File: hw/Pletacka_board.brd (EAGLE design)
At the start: 75 x 55 mm, 45 parts, among them U1 LM75BDP, U2 EL357N(A)(TA)-G, U3 EL357N(A)(TA)-G, U4 EL357N(A)(TA)-G, U5 EL357N(A)(TA)-G, U6 TPS54231D

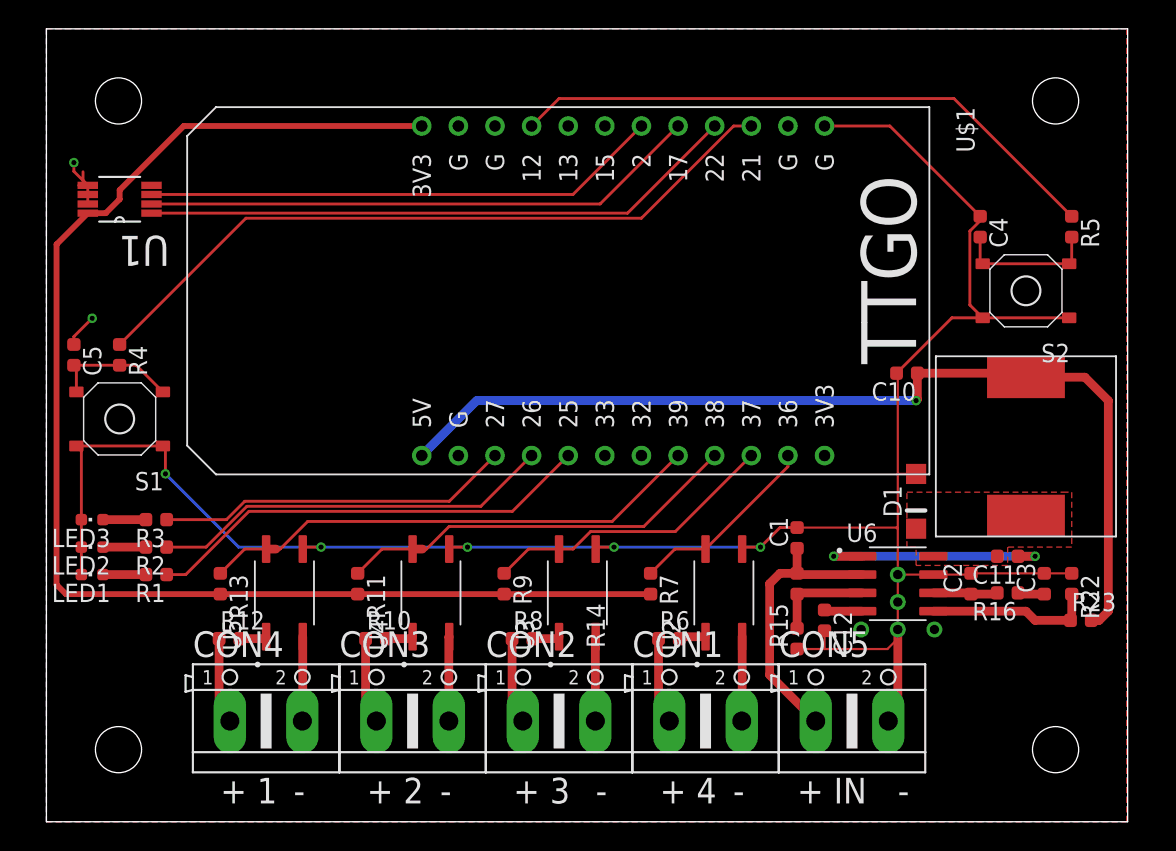
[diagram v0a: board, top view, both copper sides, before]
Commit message: Add 2 pinheads
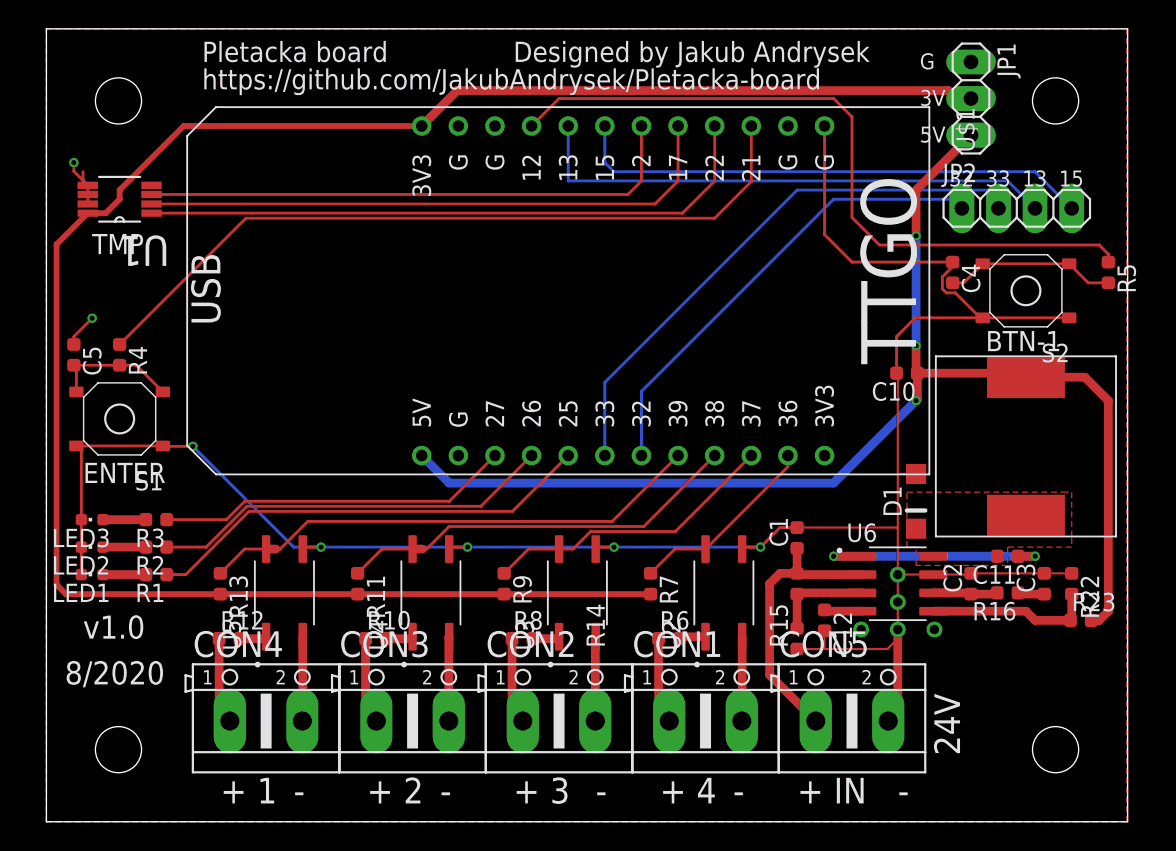
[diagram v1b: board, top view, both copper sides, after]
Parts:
- added JP1: (no value), pinhead:1X03
- added JP2: (no value), pinhead:1X04
- moved R5 4.07 mm to (73.7, 38.1)
- moved C4 3.70 mm to (62.9, 38.1)
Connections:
- removed net N$26: U$1.15
- removed net N$27: U$1.13
- removed net N$3: U$1.32
- removed net N$4: U$1.33
- new net GPIO13: JP2.3, U$1.13
- new net GPIO15: JP2.4, U$1.15
- new net GPIO32: JP2.1, U$1.32
- new net GPIO33: JP2.2, U$1.33
- net +3V3: now also JP1.2
- net +5V: now also JP1.3
- net GND: now also JP1.1
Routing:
- net +3V3: track 94.2 -> 133.5 mm
- net GPIO33: track 0.00 -> 38.8 mm
- net GPIO13: track 0.00 -> 37.0 mm
- net GPIO15: track 0.00 -> 36.2 mm
- net GPIO32: track 0.00 -> 32.5 mm
- net +5V: track 68.5 -> 88.2 mm, vias 1 -> 3
- net BUTTON2: track 41.6 -> 49.9 mm
- net BUTTON1: track 50.1 -> 52.4 mm
- net TMP_OS: track 36.0 -> 38.2 mm
- net TMP_SDA: track 41.6 -> 43.8 mm
- net TMP_SCL: track 38.8 -> 41.0 mm
- net GND: track 164.9 -> 167.1 mm
- net N$10: track 9.84 -> 11.9 mm
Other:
- board text added: "13"
- board text added: "15"
- board text added: "24V"
- board text added: "32"
- board text added: "33"
- board text added: "3V"
- board text added: "5V"
- board text added: "8/2020"
- board text added: "BTN-1"
- board text added: "Designed by Jakub Andrysek"
- board text added: "ENTER"
- board text added: "G"
- board text added: "Pletacka board"
- board text added: "TMP"
- board text added: "USB"
- board text added: "https://github.com/JakubAndrysek/Pletacka-board"
- board text added: "v1.0"

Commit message: Fix Cednik's issues
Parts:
- added D2, D4, D6: B5819W, B5819W:SOD-123
- added D3: SS34, diode:SMA
- added JP3: (no value), pinhead:1X04
- C1: value 10u -> 10u/50V; device rcl_upravena:C0603 -> rcl_upravena:C1206
- C4, C5: value 1u -> 100n
- R10, R12, R6, R8: value 1k -> 2k/0.25W; device rcl_upravena:R0603 -> rcl_upravena:R1206
- U1: value LM75BDP -> LM75BDP-NEW; device LM75BDP:SOP65P490X110-8N -> LM75BDP:SOT505-1
- moved D1 25.5 mm to (36.8, 12.3), turned to 0 degrees
- moved R13 2.69 mm to (14.0, 18.4)
- moved C1 2.07 mm to (53.6, 21.1), turned to 0 degrees
- moved R8 2.01 mm to (32.4, 14.6)
- moved U3 2.01 mm to (37.5, 17.8)
- moved R12 2.01 mm to (12.1, 14.6)
- moved R10 2.01 mm to (22.2, 14.6)
- moved R6 2.01 mm to (42.5, 14.6)
- moved U2 2.01 mm to (47.6, 17.8)
- moved U4 2.01 mm to (27.3, 17.8)
- moved U5 2.01 mm to (17.1, 17.8)
- moved R7 2.01 mm to (42.5, 18.4)
- moved R11 2.01 mm to (22.2, 18.4)
- moved R9 2.01 mm to (32.4, 18.4)
- moved R5 1.27 mm to (73.7, 36.8)
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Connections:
- net +3V3: now also U$1.3V3-2
- net GND: now also D3.A, JP3.1, JP3.2, JP3.3, JP3.4, U$1.G-2, U$1.G-3, U$1.G-4, U$1.G-5; no longer D1.A
- net N$14: now also D1.A
- net N$15: now also D1.C
- net N$17: now also D2.A
- net N$18: now also D2.C
- net N$20: now also D4.A
- net N$21: now also D4.C
- net N$7: now also D6.A
- net N$9: now also D6.C
- net PH: now also D3.C; no longer D1.C
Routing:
- net GND: track 167.1 -> 96.5 mm, vias 10 -> 12
- net +3V3: track 133.5 -> 108.0 mm
- net N$15: track 1.88 -> 5.14 mm
- net N$9: track 1.88 -> 5.14 mm
- net N$18: track 1.88 -> 5.04 mm
- net N$21: track 1.88 -> 5.04 mm
- net OPTO4: track 35.8 -> 33.3 mm
- net N$10: track 11.9 -> 14.4 mm
- net GPIO13: track 37.0 -> 34.5 mm
- net N$19: track 6.02 -> 8.50 mm
- net N$16: track 6.02 -> 8.50 mm
- net N$6: track 6.02 -> 8.50 mm
- net N$13: track 6.02 -> 8.50 mm
- net N$17: track 5.86 -> 8.22 mm
- net N$7: track 5.86 -> 8.03 mm
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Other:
- outline, holes or cut-outs redrawn
- board text added: "Designed by kubaandrysek.cz"
- board text added: "PWR"
- board text added: "SEND"
- board text added: "WIFI"
- board text removed: "BTN-1"
- board text removed: "Designed by Jakub Andrysek"

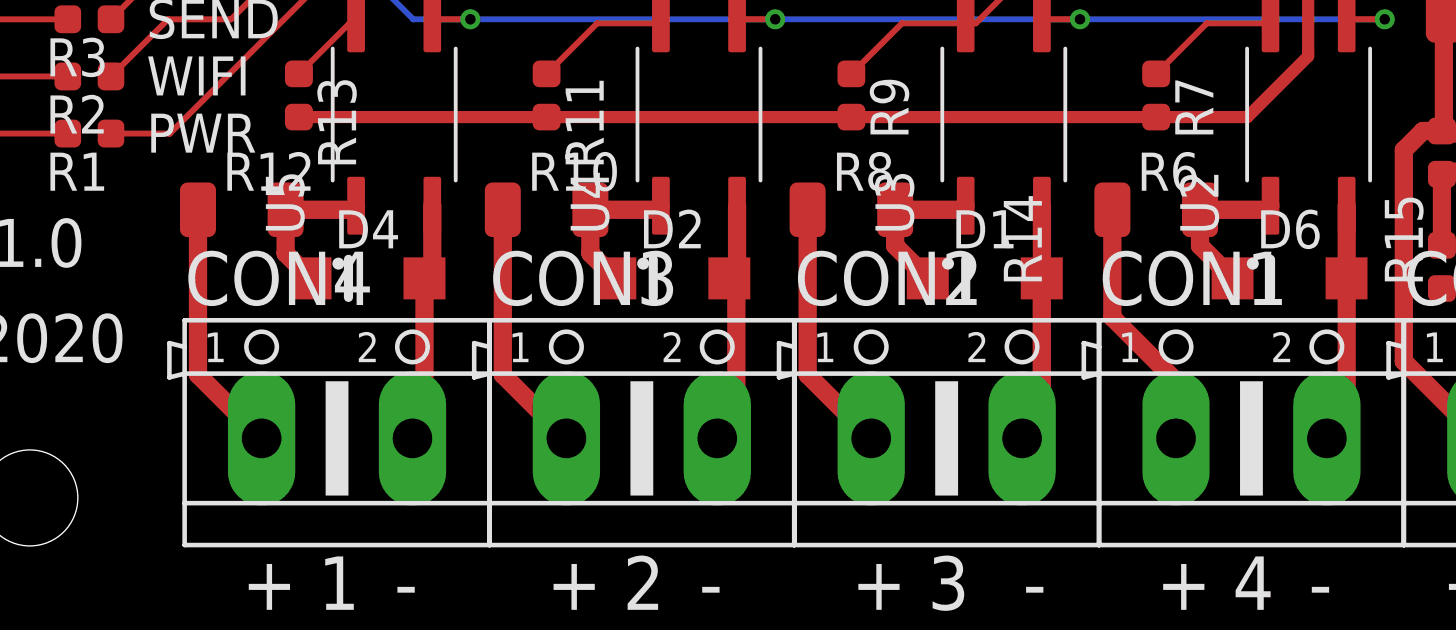
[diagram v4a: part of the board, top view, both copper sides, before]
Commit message: Change octocoupler resistor to 20k (close #2)
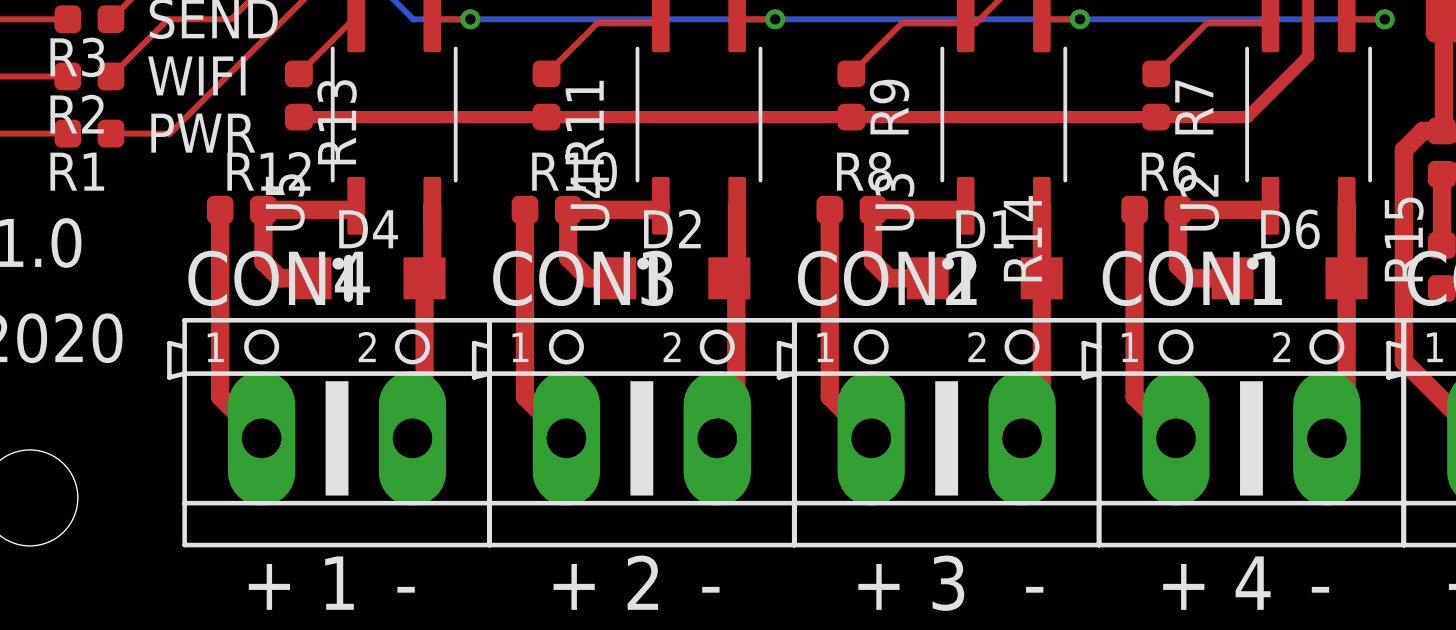
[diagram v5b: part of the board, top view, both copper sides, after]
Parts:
- R10, R12, R6, R8: value 2k/0.25W -> 20k; device rcl_upravena:R1206 -> rcl_upravena:R0603
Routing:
- net N$9: track 5.14 -> 7.01 mm
- net N$15: track 5.14 -> 6.93 mm
- net N$21: track 5.04 -> 6.68 mm
- net N$18: track 5.04 -> 6.61 mm
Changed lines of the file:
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@@
 <attribute name="VALUE" x="40.64" y="1.27" size="1.778" layer="27" ratio="10"/>
 </element>
-<element name="R6" library="rcl_upravena" package="R1206" value="2k/0.25W" x="42.545" y="14.605" smashed="yes">
-<attribute name="LCSC_ID" value="C17944" x="42.545" y="14.605" size="1.778" layer="27" display="off"/>
+<element name="R6" library="rcl_upravena" package="R0603" value="20k" x="42.545" y="14.605" smashed="yes">
+<attribute name="LCSC_ID" value="C4184" x="42.545" y="14.605" size="1.778" layer="27" display="off"/>
 <attribute name="NAME" x="41.91" y="15.24" size="1.27" layer="25"/>
 <attribute name="VALUE" x="41.91" y="12.7" size="1.27" layer="27"/>
@@
 <attribute name="VALUE" x="30.48" y="1.27" size="1.778" layer="27" ratio="10"/>
 </element>
-<element name="R8" library="rcl_upravena" package="R1206" value="2k/0.25W" x="32.385" y="14.605" smashed="yes">
-<attribute name="LCSC_ID" value="C17944" x="32.385" y="14.605" size="1.778" layer="27" display="off"/>
+<element name="R8" library="rcl_upravena" package="R0603" value="20k" x="32.385" y="14.605" smashed="yes">
+<attribute name="LCSC_ID" value="C4184" x="32.385" y="14.605" size="1.778" layer="27" display="off"/>
 <attribute name="NAME" x="31.75" y="15.24" size="1.27" layer="25"/>
 <attribute name="VALUE" x="31.75" y="12.7" size="1.27" layer="27"/>
@@
 <attribute name="VALUE" x="20.32" y="1.27" size="1.778" layer="27" ratio="10"/>
 </element>
-<element name="R10" library="rcl_upravena" package="R1206" value="2k/0.25W" x="22.225" y="14.605" smashed="yes">
-<attribute name="LCSC_ID" value="C17944" x="22.225" y="14.605" size="1.778" layer="27" display="off"/>
+<element name="R10" library="rcl_upravena" package="R0603" value="20k" x="22.225" y="14.605" smashed="yes">
+<attribute name="LCSC_ID" value="C4184" x="22.225" y="14.605" size="1.778" layer="27" display="off"/>
 <attribute name="NAME" x="21.59" y="15.24" size="1.27" layer="25"/>
 <attribute name="VALUE" x="21.59" y="12.7" size="1.27" layer="27"/>
@@
 <attribute name="VALUE" x="10.16" y="1.27" size="1.778" layer="27" ratio="10"/>
 </element>
-<element name="R12" library="rcl_upravena" package="R1206" value="2k/0.25W" x="12.065" y="14.605" smashed="yes">
-<attribute name="LCSC_ID" value="C17944" x="12.065" y="14.605" size="1.778" layer="27" display="off"/>
+<element name="R12" library="rcl_upravena" package="R0603" value="20k" x="12.065" y="14.605" smashed="yes">
+<attribute name="LCSC_ID" value="C4184" x="12.065" y="14.605" size="1.778" layer="27" display="off"/>
 <attribute name="NAME" x="11.43" y="15.24" size="1.27" layer="25"/>
 <attribute name="VALUE" x="11.43" y="12.7" size="1.27" layer="27"/>
@@
 <contactref element="CON1" pad="1"/>
 <contactref element="R6" pad="1"/>
-<wire x1="43.2054" y1="8.893990625" x2="43.2054" y2="6.985" width="0.6096" layer="1"/>
-<wire x1="41.085" y1="14.605" x2="41.085" y2="11.014390625" width="0.6096" layer="1"/>
-<wire x1="41.085" y1="11.014390625" x2="43.2054" y2="8.893990625" width="0.6096" layer="1"/>
+<wire x1="43.2054" y1="6.985" x2="41.825" y2="8.3654" width="0.6096" layer="1"/>
+<wire x1="41.825" y1="8.3654" x2="41.825" y2="14.605" width="0.6096" layer="1"/>
 </signal>
 <signal name="N$7">
@@
 <contactref element="D6" pad="C"/>
 <wire x1="46.355" y1="14.74" x2="46.22" y2="14.605" width="0.6096" layer="1"/>
-<wire x1="46.22" y1="14.605" x2="44.005" y2="14.605" width="0.6096" layer="1"/>
-<wire x1="44.005" y1="14.605" x2="44.005" y2="13.404" width="0.6096" layer="1"/>
-<wire x1="44.005" y1="13.404" x2="45.09" y2="12.319" width="0.6096" layer="1"/>
+<wire x1="46.22" y1="14.605" x2="43.265" y2="14.605" width="0.6096" layer="1"/>
+<wire x1="45.09" y1="12.319" x2="43.688" y2="12.319" width="0.6096" layer="1"/>
+<wire x1="43.265" y1="12.742" x2="43.265" y2="14.605" width="0.6096" layer="1"/>
+<wire x1="43.688" y1="12.319" x2="43.265" y2="12.742" width="0.6096" layer="1"/>
 </signal>
 <signal name="N$13">
 <contactref element="CON2" pad="1"/>
 <contactref element="R8" pad="1"/>
-<wire x1="30.925" y1="14.605" x2="30.925" y2="9.1054" width="0.6096" layer="1"/>
-<wire x1="30.925" y1="9.1054" x2="33.0454" y2="6.985" width="0.6096" layer="1"/>
+<wire x1="33.0454" y1="6.985" x2="31.665" y2="8.3654" width="0.6096" layer="1"/>
+<wire x1="31.665" y1="8.3654" x2="31.665" y2="14.605" width="0.6096" layer="1"/>
 </signal>
 <signal name="N$14">
@@
 <contactref element="U3" pad="1"/>
 <wire x1="36.195" y1="14.74" x2="36.06" y2="14.605" width="0.6096" layer="1"/>
-<wire x1="36.06" y1="14.605" x2="33.845" y2="14.605" width="0.6096" layer="1"/>
+<wire x1="36.06" y1="14.605" x2="33.105" y2="14.605" width="0.6096" layer="1"/>
 <contactref element="D1" pad="C"/>
-<wire x1="33.845" y1="14.605" x2="33.845" y2="13.404" width="0.6096" layer="1"/>
-<wire x1="33.845" y1="13.404" x2="34.93" y2="12.319" width="0.6096" layer="1"/>
+<wire x1="34.93" y1="12.319" x2="33.655" y2="12.319" width="0.6096" layer="1"/>
+<wire x1="33.105" y1="12.869" x2="33.105" y2="14.605" width="0.6096" layer="1"/>
+<wire x1="33.655" y1="12.319" x2="33.105" y2="12.869" width="0.6096" layer="1"/>
 </signal>
 <signal name="N$16">
 <contactref element="CON3" pad="1"/>
 <contactref element="R10" pad="1"/>
-<wire x1="20.765" y1="14.605" x2="20.765" y2="9.1054" width="0.6096" layer="1"/>
-<wire x1="20.765" y1="9.1054" x2="22.8854" y2="6.985" width="0.6096" layer="1"/>
+<wire x1="21.505" y1="14.605" x2="21.505" y2="8.3654" width="0.6096" layer="1"/>
+<wire x1="21.505" y1="8.3654" x2="22.8854" y2="6.985" width="0.6096" layer="1"/>
 </signal>
 <signal name="N$17">
@@
 <contactref element="D2" pad="C"/>
 <wire x1="26.035" y1="14.74" x2="25.9" y2="14.605" width="0.6096" layer="1"/>
-<wire x1="25.9" y1="14.605" x2="23.685" y2="14.605" width="0.6096" layer="1"/>
-<wire x1="23.685" y1="14.605" x2="23.685" y2="13.15" width="0.6096" layer="1"/>
-<wire x1="23.685" y1="13.15" x2="24.516" y2="12.319" width="0.6096" layer="1"/>
+<wire x1="25.9" y1="14.605" x2="22.945" y2="14.605" width="0.6096" layer="1"/>
+<wire x1="24.516" y1="12.319" x2="23.622" y2="12.319" width="0.6096" layer="1"/>
+<wire x1="22.945" y1="12.996" x2="22.945" y2="14.605" width="0.6096" layer="1"/>
+<wire x1="23.622" y1="12.319" x2="22.945" y2="12.996" width="0.6096" layer="1"/>
 </signal>
 <signal name="N$19">
 <contactref element="CON4" pad="1"/>
 <contactref element="R12" pad="1"/>
-<wire x1="10.605" y1="14.605" x2="10.605" y2="9.1054" width="0.6096" layer="1"/>
-<wire x1="10.605" y1="9.1054" x2="12.7254" y2="6.985" width="0.6096" layer="1"/>
+<wire x1="12.7254" y1="6.985" x2="11.345" y2="8.3654" width="0.6096" layer="1"/>
+<wire x1="11.345" y1="8.3654" x2="11.345" y2="14.605" width="0.6096" layer="1"/>
 </signal>
 <signal name="N$20">
@@
 <contactref element="D4" pad="C"/>
 <wire x1="15.875" y1="14.74" x2="15.74" y2="14.605" width="0.6096" layer="1"/>
-<wire x1="15.74" y1="14.605" x2="13.525" y2="14.605" width="0.6096" layer="1"/>
-<wire x1="13.525" y1="14.605" x2="13.525" y2="13.15" width="0.6096" layer="1"/>
-<wire x1="13.525" y1="13.15" x2="14.356" y2="12.319" width="0.6096" layer="1"/>
+<wire x1="15.74" y1="14.605" x2="12.785" y2="14.605" width="0.6096" layer="1"/>
+<wire x1="14.356" y1="12.319" x2="13.335" y2="12.319" width="0.6096" layer="1"/>
+<wire x1="12.785" y1="12.869" x2="12.785" y2="14.605" width="0.6096" layer="1"/>
+<wire x1="13.335" y1="12.319" x2="12.785" y2="12.869" width="0.6096" layer="1"/>
 </signal>
 <signal name="VIN">

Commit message: Change step-down voltage (close #4)
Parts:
- R22: value 1.8k -> 6k8
- R23: value 10k -> 36k
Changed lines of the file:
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@@
 <attribute name="VALUE" x="60.325" y="33.02" size="1.27" layer="27" rot="R180"/>
 </element>
-<element name="R22" library="rcl_upravena" package="R0603" value="1.8k" x="71.12" y="16.51" smashed="yes" rot="R270">
-<attribute name="LCSC_ID" value="C4177" x="71.12" y="16.51" size="1.778" layer="27" rot="R270" display="off"/>
+<element name="R22" library="rcl_upravena" package="R0603" value="6k8" x="71.12" y="16.51" smashed="yes" rot="R270">
+<attribute name="LCSC_ID" value="C23212" x="71.12" y="16.51" size="1.778" layer="27" rot="R270" display="off"/>
 <attribute name="NAME" x="71.755" y="17.145" size="1.27" layer="25" rot="R270"/>
 <attribute name="VALUE" x="69.215" y="17.145" size="1.27" layer="27" rot="R270"/>
 </element>
-<element name="R23" library="rcl_upravena" package="R0603" value="10k" x="71.755" y="13.97" smashed="yes">
-<attribute name="LCSC_ID" value="C25804" x="71.755" y="13.97" size="1.778" layer="27" display="off"/>
+<element name="R23" library="rcl_upravena" package="R0603" value="36k" x="71.755" y="13.97" smashed="yes">
+<attribute name="LCSC_ID" value="C23147" x="71.755" y="13.97" size="1.778" layer="27" display="off"/>
 <attribute name="NAME" x="71.12" y="14.605" size="1.27" layer="25"/>
 <attribute name="VALUE" x="71.12" y="12.065" size="1.27" layer="27"/>
